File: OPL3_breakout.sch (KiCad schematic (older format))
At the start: 7 parts, among them J1 Conn_01x10, J2 Conn_01x10, J3 Conn_01x02, J4 Conn_01x02, U1 YMF262-M, U2 YAC512-M

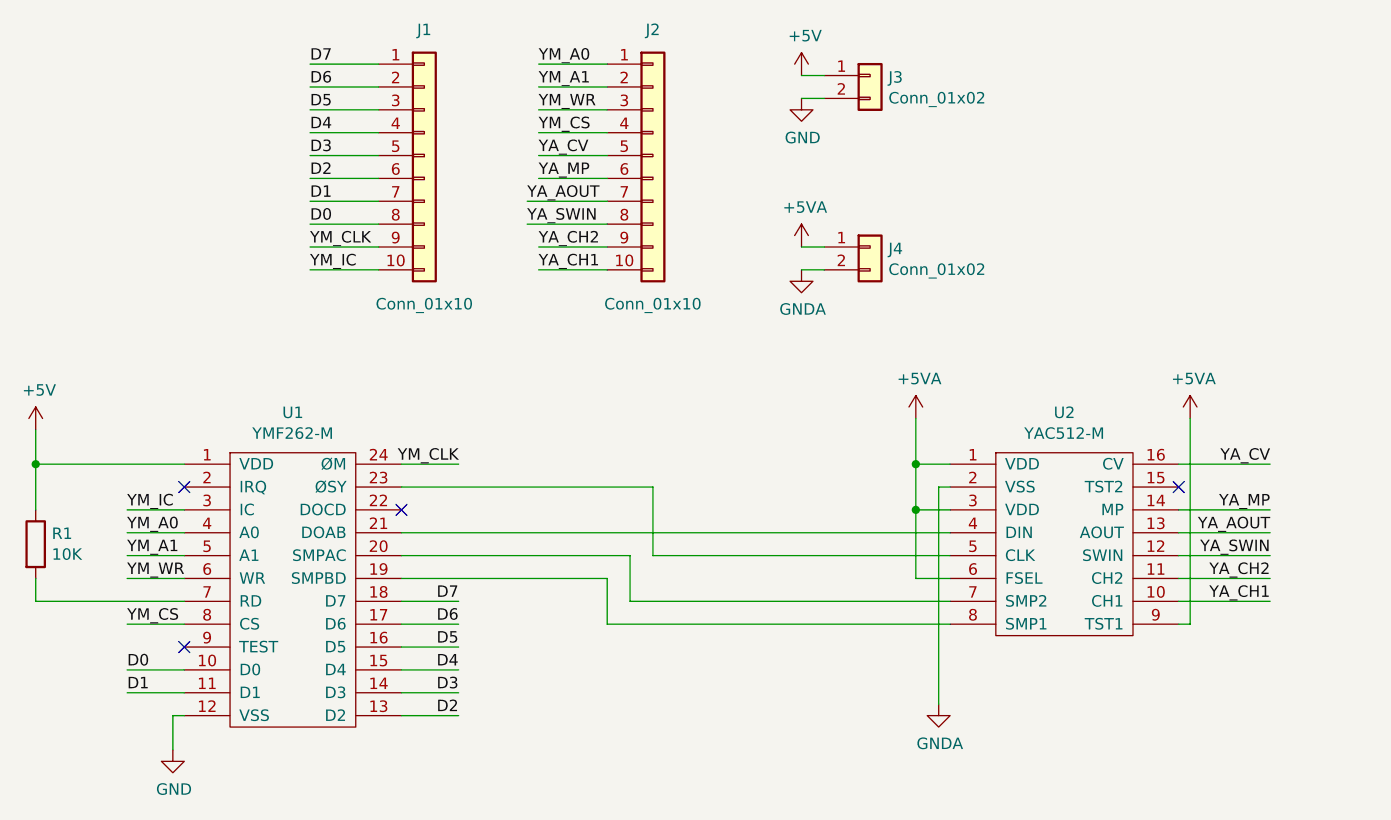
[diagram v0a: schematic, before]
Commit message: add test points
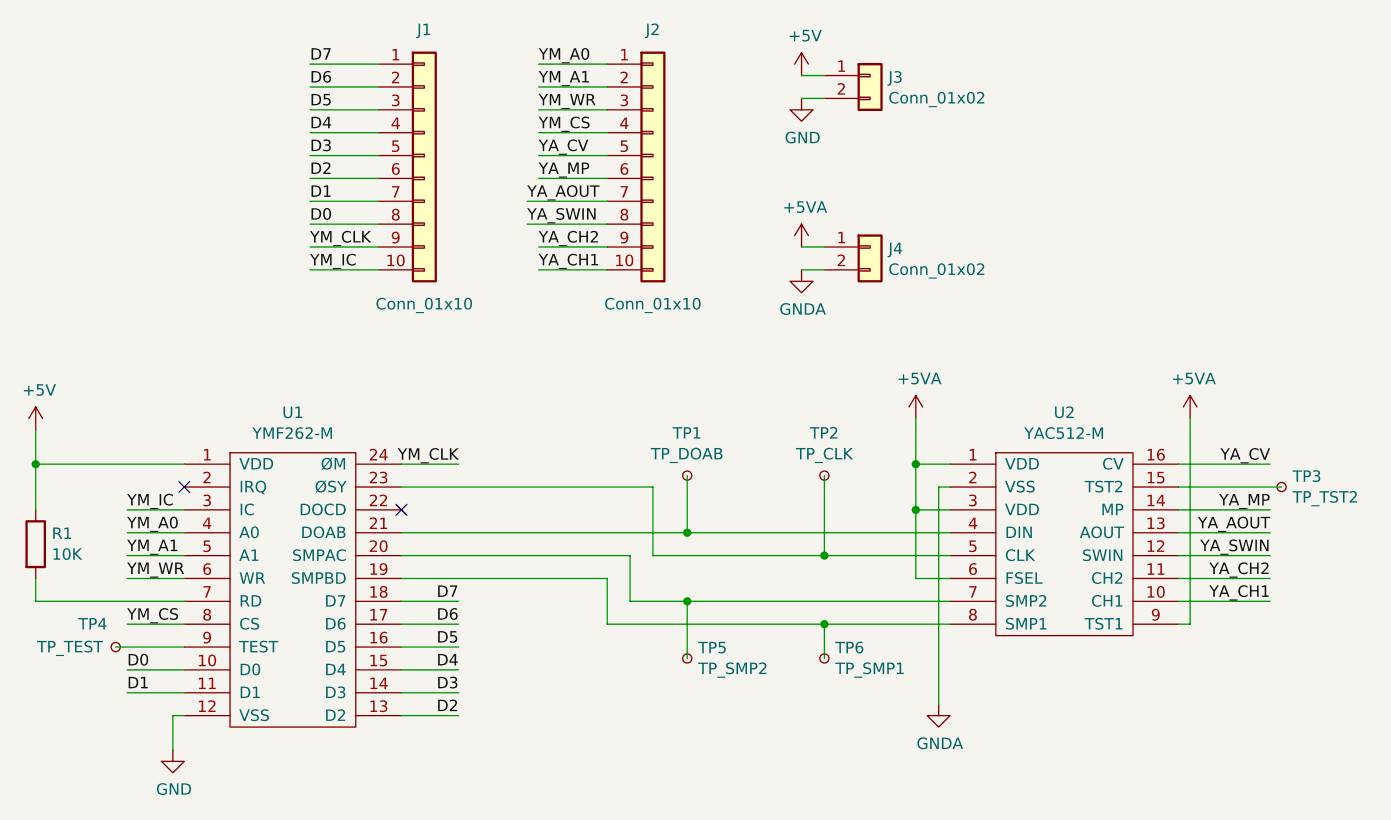
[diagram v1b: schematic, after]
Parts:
- added TP1: TP_DOAB, TestPoint:TestPoint_Keystone_5000-5004_Miniature, symbol Connector:TestPoint_Small
- added TP2: TP_CLK, TestPoint:TestPoint_Keystone_5000-5004_Miniature, symbol Connector:TestPoint_Small
- added TP3: TP_TST2, TestPoint:TestPoint_Keystone_5000-5004_Miniature, symbol Connector:TestPoint_Small
- added TP4: TP_TEST, TestPoint:TestPoint_Keystone_5000-5004_Miniature, symbol Connector:TestPoint_Small
- added TP5: TP_SMP2, TestPoint:TestPoint_Keystone_5000-5004_Miniature, symbol Connector:TestPoint_Small
- added TP6: TP_SMP1, TestPoint:TestPoint_Keystone_5000-5004_Miniature, symbol Connector:TestPoint_Small
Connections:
- net at U2.15 (TST2): now also TP3.1
- net at U1.21 (DOAB), U2.4 (DIN): now also TP1.1
- net at U1.23 (ØSY), U2.5 (CLK): now also TP2.1
- net at U1.20 (SMPAC), U2.7 (SMP2): now also TP5.1
- net at U1.19 (SMPBD), U2.8 (SMP1): now also TP6.1
- net at U1.9 (TEST): now also TP4.1
- no-connect marks 4 -> 2
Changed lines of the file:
@@
 $EndDescr
-$Comp
-L OPL3:YAC512-M U2
-U 1 1 5FE3D104
-P 6650 3550
-F 0 "U2" H 7150 3775 50  0000 C CNN
-F 1 "YAC512-M" H 7150 3684 50  0000 C CNN
-F 2 "OPL3:SOP127P780X200-16N" H 7050 3650 50  0001 C CNN
-F 3 "" H 7050 3650 50  0001 C CNN
-	1    6650 3550
-	1    0    0    -1
-$EndComp
 $Comp
 L OPL3:YMF262-M U1
@@
 	4250 3650 5350 3650
 Wire Wire Line
-	5350 3950 6650 3950
+	5350 3950 6100 3950
 Wire Wire Line
 	5350 3950 5350 3650
 Wire Wire Line
-	4250 3850 6650 3850
+	4250 3850 5500 3850
 $Comp
 L power:GNDA #PWR0103
@@
 	4250 3950 5250 3950
 Wire Wire Line
-	5250 4150 6650 4150
+	5250 4150 5500 4150
 Wire Wire Line
 	6500 3750 6500 4050
@@
 	4250 4050 5150 4050
 Wire Wire Line
-	5150 4250 6650 4250
+	5150 4250 6100 4250
 Text Label 4500 4150 2    50   ~ 0
 D7
@@
 Text Label 3050 4450 0    50   ~ 0
 D0
-NoConn ~ 3300 4350
 Text Label 3050 4250 0    50   ~ 0
 YM_CS
@@
 Wire Wire Line
 	2650 4150 3300 4150
-NoConn ~ 7650 3650
 Wire Wire Line
 	7700 4250 7700 3350
@@
 Wire Wire Line
 	6100 2700 6000 2700
+$Comp
+L Connector:TestPoint_Small TP1
+U 1 1 5FFA06B6
+P 5500 3600
+F 0 "TP1" V 5685 3600 50  0000 C CNN
+F 1 "TP_DOAB" V 5594 3600 50  0000 C CNN
+F 2 "TestPoint:TestPoint_Keystone_5000-5004_Miniature" H 5700 3600 50  0001 C CNN
+F 3 "~" H 5700 3600 50  0001 C CNN
+	1    5500 3600
+	0    -1   -1   0
+$EndComp
+$Comp
+L Connector:TestPoint_Small TP2
+U 1 1 5FFA400A
+P 6100 3600
+F 0 "TP2" V 6285 3600 50  0000 C CNN
+F 1 "TP_CLK" V 6194 3600 50  0000 C CNN
+F 2 "TestPoint:TestPoint_Keystone_5000-5004_Miniature" H 6300 3600 50  0001 C CNN
+F 3 "~" H 6300 3600 50  0001 C CNN
+	1    6100 3600
+	0    -1   -1   0
+$EndComp
+$Comp
+L Connector:TestPoint_Small TP6
+U 1 1 5FFA75A2
+P 6100 4400
+F 0 "TP6" V 6054 4448 50  0000 L CNN
+F 1 "TP_SMP1" V 6145 4448 50  0000 L CNN
+F 2 "TestPoint:TestPoint_Keystone_5000-5004_Miniature" H 6300 4400 50  0001 C CNN
+F 3 "~" H 6300 4400 50  0001 C CNN
+	1    6100 4400
+	0    1    1    0
+$EndComp
+$Comp
+L Connector:TestPoint_Small TP5
+U 1 1 5FFA75A8
+P 5500 4400
+F 0 "TP5" V 5454 4448 50  0000 L CNN
+F 1 "TP_SMP2" V 5545 4448 50  0000 L CNN
+F 2 "TestPoint:TestPoint_Keystone_5000-5004_Miniature" H 5700 4400 50  0001 C CNN
+F 3 "~" H 5700 4400 50  0001 C CNN
+	1    5500 4400
+	0    1    1    0
+$EndComp
+Wire Wire Line
+	6100 4400 6100 4250
+Connection ~ 6100 4250
+Wire Wire Line
+	6100 4250 6650 4250
+Wire Wire Line
+	5500 4400 5500 4150
+Connection ~ 5500 4150
+Wire Wire Line
+	5500 4150 6650 4150
+Wire Wire Line
+	5500 3600 5500 3850
+Connection ~ 5500 3850
+Wire Wire Line
+	5500 3850 6650 3850
+Wire Wire Line
+	6100 3600 6100 3950
+Connection ~ 6100 3950
+Wire Wire Line
+	6100 3950 6650 3950
+Wire Wire Line
+	3000 4350 3300 4350
+$Comp
+L OPL3:YAC512-M U2
+U 1 1 5FE3D104
+P 6650 3550
+F 0 "U2" H 7150 3775 50  0000 C CNN
+F 1 "YAC512-M" H 7150 3684 50  0000 C CNN
+F 2 "OPL3:SOP127P780X200-16N" H 7050 3650 50  0001 C CNN
+F 3 "" H 7050 3650 50  0001 C CNN
+	1    6650 3550
+	1    0    0    -1
+$EndComp
+Wire Wire Line
+	7650 3650 8100 3650
+$Comp
+L Connector:TestPoint_Small TP3
+U 1 1 5FFC6402
+P 8100 3650
+F 0 "TP3" H 8148 3696 50  0000 L CNN
+F 1 "TP_TST2" H 8148 3605 50  0000 L CNN
+F 2 "TestPoint:TestPoint_Keystone_5000-5004_Miniature" H 8300 3650 50  0001 C CNN
+F 3 "~" H 8300 3650 50  0001 C CNN
+	1    8100 3650
+	1    0    0    -1
+$EndComp
+$Comp
+L Connector:TestPoint_Small TP4
+U 1 1 5FFBB2DA
+P 3000 4350
+F 0 "TP4" H 2900 4250 50  0000 C CNN
+F 1 "TP_TEST" H 2800 4350 50  0000 C CNN
+F 2 "TestPoint:TestPoint_Keystone_5000-5004_Miniature" H 3200 4350 50  0001 C CNN
+F 3 "~" H 3200 4350 50  0001 C CNN
+	1    3000 4350
+	1    0    0    1
+$EndComp
 $EndSCHEMATC
